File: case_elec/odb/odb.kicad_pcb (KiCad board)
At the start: 2 copper layers, 98 x 79 mm, 10 parts, among them J1 Screw_Terminal_01x02, J2 Conn_02x07_Top_Bottom, SW1 SW_SPST, SW2 SW_SPST, U1 REYAX RYLR896, U2 BNO055, U3 MPL3115A, U4 Ultimate_GPS, U5 Teensy3.5

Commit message: Ajout de pistes B.Cu
Alternative à :
- resistances 0 Ohm
- modification du pinout de la Teensy 3.5

Attention : les gerbers n'ont pas été générés.
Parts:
- removed R1: RESISTOR_1206, Resistor_SMD:R_1206_3216Metric_Pad1.30x1.75mm_HandSolder
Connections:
- U3 pad 6: Net-(U2-Pad5) -> unconnected-(U3-Pad6)
- U4 pad 5: Net-(R1-Pad1) -> Net-(U4-Pad5)
- U4 pad 6: unconnected-(U4-Pad6) -> Net-(U4-Pad6)
- U5 pad 2: Net-(R1-Pad2) -> Net-(U4-Pad5)
- U5 pad 3: unconnected-(U5-Pad3) -> Net-(U4-Pad6)
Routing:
- net Net-(U4-Pad5): track 0.00 -> 11.5 mm
- net unconnected-(U5-Pad3): track 9.36 -> 0.00 mm
- net Net-(U4-Pad6): track 0.00 -> 9.36 mm
- net +5V: track 177.4 -> 168.9 mm
- net Net-(R1-Pad1): track 6.25 -> 0.00 mm
- net Net-(R1-Pad2): track 3.93 -> 0.00 mm
- net Net-(U2-Pad5): track 66.5 -> 64.9 mm

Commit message: Amélioration tracé pistes
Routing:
- net Net-(U4-Pad5): track 11.5 -> 14.4 mm
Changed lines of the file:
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@@
     (pts (xy 198.247 56.769) (xy 198.247 135.769))
     (height -7.493)
-    (gr_text "79.0000 mm" (at 204.59 96.269 90) (layer "User.1")
+    (gr_text "79,0000 mm" (at 204.59 96.269 90) (layer "User.1")
       (effects (font (size 1 1) (thickness 0.15)))
     )
@@
     (pts (xy 100.203 56.769) (xy 198.247 56.769))
     (height -5.969)
-    (gr_text "98.0440 mm" (at 149.225 49.65) (layer "User.1")
+    (gr_text "98,0440 mm" (at 149.225 49.65) (layer "User.1")
       (effects (font (size 1 1) (thickness 0.15)))
     )
@@
     (pts (xy 198.374 135.89) (xy 198.374 131.318))
     (height 12.954)
-    (gr_text "4.5720 mm" (at 210.178 133.604 90) (layer "User.1")
+    (gr_text "4,5720 mm" (at 210.178 133.604 90) (layer "User.1")
       (effects (font (size 1 1) (thickness 0.15)))
     )
@@
   (segment (start 144.074067 70.454442) (end 144.806125 71.1865) (width 0.4) (layer "F.Cu") (net 35))
   (segment (start 150.642058 71.1865) (end 152.4 72.944442) (width 0.4) (layer "F.Cu") (net 35))
-  (segment (start 152.4 75.484442) (end 144.83 67.914442) (width 0.4) (layer "B.Cu") (net 76))
-  (segment (start 144.83 67.914442) (end 144.074067 67.914442) (width 0.4) (layer "B.Cu") (net 76))
+  (segment (start 149.144442 75.484442) (end 152.4 75.484442) (width 0.4) (layer "B.Cu") (net 76))
+  (segment (start 146.654442 67.914442) (end 147.32 68.58) (width 0.4) (layer "B.Cu") (net 76))
+  (segment (start 144.074067 67.914442) (end 146.654442 67.914442) (width 0.4) (layer "B.Cu") (net 76))
+  (segment (start 147.32 73.66) (end 149.144442 75.484442) (width 0.4) (layer "B.Cu") (net 76))
+  (segment (start 147.32 68.58) (end 147.32 73.66) (width 0.4) (layer "B.Cu") (net 76))
   (zone (net 2) (net_name "GND") (layer "F.Cu") (name "plan de masse") (hatch edge 0.508)
     (connect_pads (clearance 0.508))

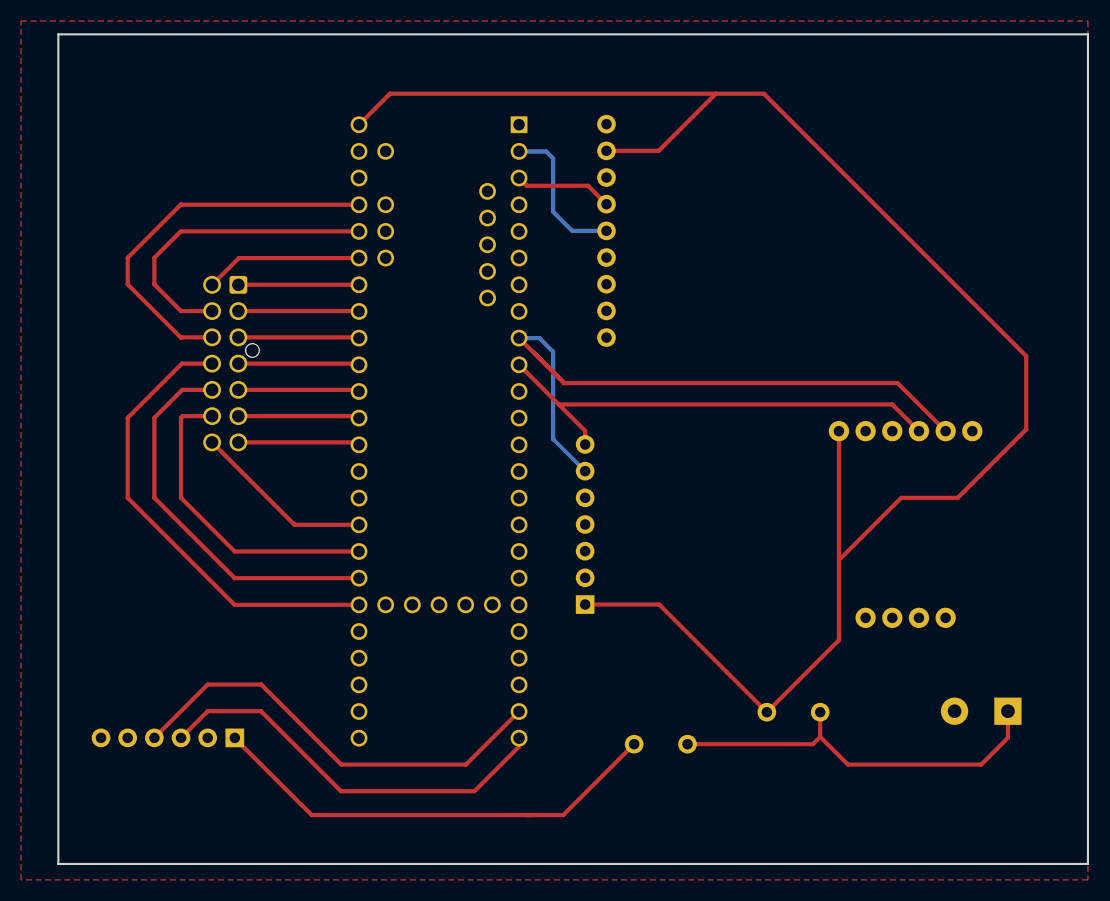
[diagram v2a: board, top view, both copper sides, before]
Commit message: Ajout du plan de masse sur l'autre layer
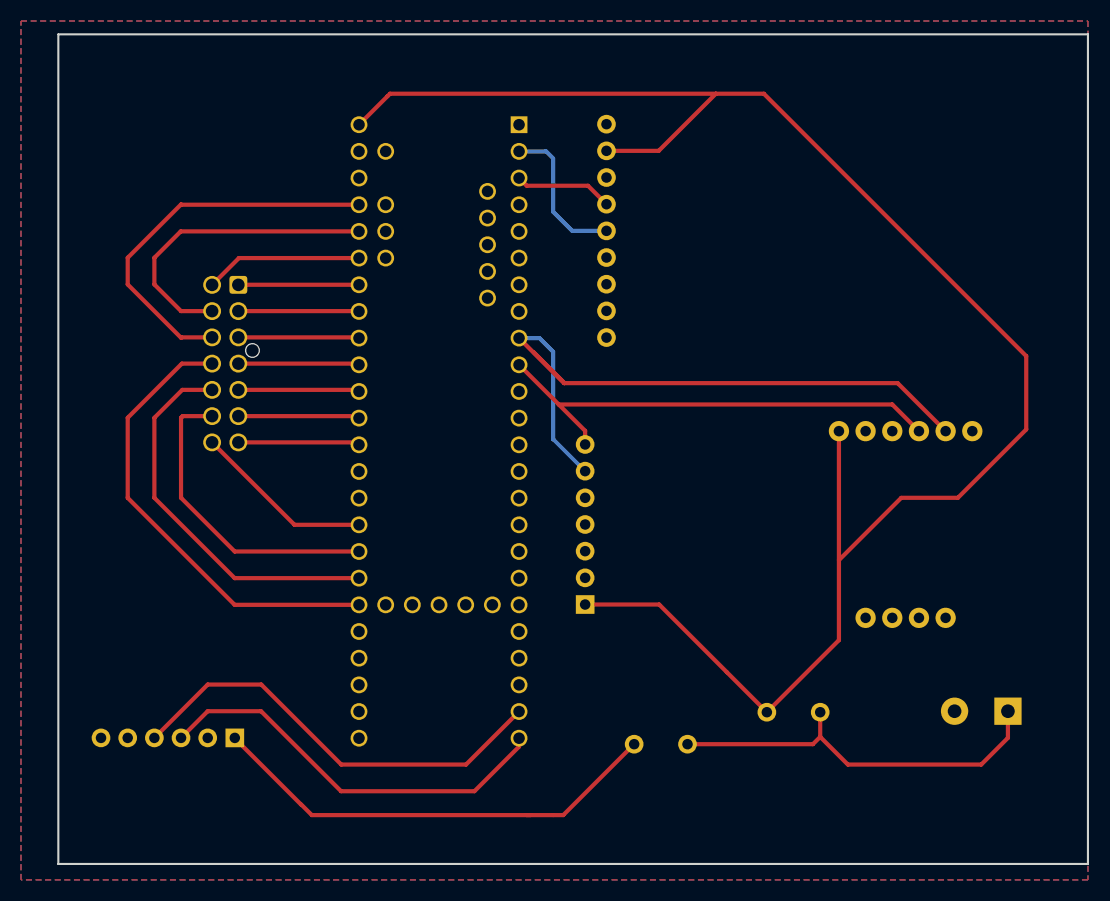
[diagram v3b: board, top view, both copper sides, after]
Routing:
- added copper zone on B.Cu, net GND
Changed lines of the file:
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@@
   (segment (start 147.32 73.66) (end 149.144442 75.484442) (width 0.4) (layer "B.Cu") (net 76))
   (segment (start 147.32 68.58) (end 147.32 73.66) (width 0.4) (layer "B.Cu") (net 76))
-  (zone (net 2) (net_name "GND") (layer "F.Cu") (name "plan de masse") (hatch edge 0.508)
+  (zone (net 2) (net_name "GND") (layers F&B.Cu) (name "plan de masse") (hatch edge 0.508)
     (connect_pads (clearance 0.508))
     (min_thickness 0.254) (filled_areas_thickness no)
